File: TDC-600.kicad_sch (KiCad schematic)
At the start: 32 parts, among them J1 MSXCART1, J2 Conn_01x03_Male, J3 Conn_01x03_Male, J4 Conn_01x03_Male, J5 Conn_01x03_Male, J6 FDD Connector, J7 ROM_SWITCH, SW1 SW_Push, U1 AT28C256, U2 74LS04, U3 74LS138, U4 WDC37C65, Y1 16Mhz

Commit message: Routing Release 1.0
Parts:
- J1: footprint Roni Footprints:MSX_CART_SW_Official_3Holes -> Roni_Footprints:MSX_CART_SW_Official
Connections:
- net GNDREF: now also J1.41 (GND@1), J1.43 (GND@2)
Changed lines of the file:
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@@
   (junction (at 203.581 92.71) (diameter 0) (color 0 0 0 0)
   )
-  (junction (at 60.9838 78.867) (diameter 0) (color 0 0 0 0)
+  (junction (at 61.9643 78.867) (diameter 0) (color 0 0 0 0)
   )
   (junction (at 193.04 66.294) (diameter 0) (color 0 0 0 0)
@@
   (junction (at 193.04 71.374) (diameter 0) (color 0 0 0 0)
   )
+  (junction (at 66.04 78.74) (diameter 0) (color 0 0 0 0)
+  )
   (junction (at 228.346 125.857) (diameter 0) (color 0 0 0 0)
   )
@@
   )
   (junction (at 70.358 84.074) (diameter 0) (color 0 0 0 0)
-  )
-  (junction (at 60.96 78.74) (diameter 0) (color 0 0 0 0)
   )
   (junction (at 85.598 42.164) (diameter 0) (color 0 0 0 0)
@@
     (stroke (width 0) (type default) (color 0 0 0 0))
   )
-  (wire (pts (xy 58.928 78.867) (xy 60.9838 78.867))
-    (stroke (width 0) (type default) (color 0 0 0 0))
-  )
   (wire (pts (xy 129.286 105.664) (xy 121.666 105.664))
     (stroke (width 0) (type default) (color 0 0 0 0))
@@
     (stroke (width 0) (type default) (color 0 0 0 0))
   )
-  (wire (pts (xy 58.928 81.407) (xy 60.9838 81.407))
+  (wire (pts (xy 58.928 81.407) (xy 61.9643 81.407))
+    (stroke (width 0) (type default) (color 0 0 0 0))
+  )
+  (wire (pts (xy 66.04 78.867) (xy 66.04 78.74))
     (stroke (width 0) (type default) (color 0 0 0 0))
   )
@@
     (stroke (width 0) (type default) (color 0 0 0 0))
   )
-  (wire (pts (xy 60.9838 81.407) (xy 60.9838 78.867))
+  (wire (pts (xy 58.928 78.867) (xy 61.9643 78.867))
     (stroke (width 0) (type default) (color 0 0 0 0))
   )
@@
     (stroke (width 0) (type default) (color 0 0 0 0))
   )
+  (wire (pts (xy 61.9643 81.407) (xy 61.9643 78.867))
+    (stroke (width 0) (type default) (color 0 0 0 0))
+  )
   (wire (pts (xy 215.392 125.857) (xy 220.345 125.857))
     (stroke (width 0) (type default) (color 0 0 0 0))
@@
     (stroke (width 0) (type default) (color 0 0 0 0))
   )
+  (wire (pts (xy 61.9643 78.867) (xy 66.04 78.867))
+    (stroke (width 0) (type default) (color 0 0 0 0))
+  )
   (wire (pts (xy 165.354 145.161) (xy 178.054 145.161))
     (stroke (width 0) (type default) (color 0 0 0 0))
@@
     (stroke (width 0) (type default) (color 0 0 0 0))
   )
-  (wire (pts (xy 64.262 78.74) (xy 64.262 78.994))
-    (stroke (width 0) (type default) (color 0 0 0 0))
-  )
   (wire (pts (xy 122.174 132.588) (xy 122.174 130.048))
     (stroke (width 0) (type default) (color 0 0 0 0))
@@
   )
   (wire (pts (xy 108.204 137.668) (xy 109.474 137.668))
-    (stroke (width 0) (type default) (color 0 0 0 0))
-  )
-  (wire (pts (xy 60.96 78.74) (xy 64.262 78.74))
     (stroke (width 0) (type default) (color 0 0 0 0))
   )
@@
     (pin "1")
   )
-  (symbol (lib_id "power:GNDREF") (at 64.262 78.994 0) (unit 1)
-    (in_bom yes) (on_board yes) (fields_autoplaced)
-    (property "Reference" "#PWR01" (id 0) (at 64.262 85.344 0)
-      (effects (font (size 1 1)) hide)
-    )
-    (property "Value" "GNDREF" (id 1) (at 64.262 84.582 0)
-      (effects (font (size 1 1)) hide)
-    )
-    (property "Footprint" "" (id 2) (at 64.262 78.994 0)
-      (effects (font (size 1 1)) hide)
-    )
-    (property "Datasheet" "" (id 3) (at 64.262 78.994 0)
-      (effects (font (size 1 1)) hide)
-    )
-    (pin "1")
-  )
   (symbol (lib_id "power:GNDREF") (at 167.386 83.058 0) (unit 1)
     (in_bom yes) (on_board yes) (fields_autoplaced)
@@
       (effects (font (size 1 1)) hide)
     )
-    (property "Footprint" "Roni Footprints:MSX_CART_SW_Official_3Holes" (id 2) (at 43.688 58.547 0)
+    (property "Footprint" "Roni_Footprints:MSX_CART_SW_Official" (id 2) (at 43.688 58.547 0)
       (effects (font (size 1 1)) hide)
     )
@@
     (pin "7")
   )
+  (symbol (lib_id "power:GNDREF") (at 66.04 78.74 0) (unit 1)
+    (in_bom yes) (on_board yes) (fields_autoplaced)
+    (property "Reference" "#PWR?" (id 0) (at 66.04 85.09 0)
+      (effects (font (size 1 1)) hide)
+    )
+    (property "Value" "GNDREF" (id 1) (at 66.04 84.328 0)
+      (effects (font (size 1 1)) hide)
+    )
+    (property "Footprint" "" (id 2) (at 66.04 78.74 0)
+      (effects (font (size 1 1)) hide)
+    )
+    (property "Datasheet" "" (id 3) (at 66.04 78.74 0)
+      (effects (font (size 1 1)) hide)
+    )
+    (pin "1")
+  )
   (symbol (lib_id "74xx:74LS04") (at 251.206 50.8 0) (unit 1)
     (in_bom yes) (on_board yes)
@@
   )
   (symbol_instances
-    (path "/5fd49dc5-3ef7-42c3-ba98-39fb50cf0473"
-      (reference "#PWR01") (unit 1) (value "GNDREF") (footprint "")
-    )
     (path "/64de7322-3492-44c0-b600-8a8a1cbeb091"
       (reference "#PWR02") (unit 1) (value "+5V") (footprint "")
@@
       (reference "#PWR021") (unit 1) (value "+5V") (footprint "")
     )
+    (path "/f82b494c-be8d-4f2a-a5d0-8b689b314ae2"
+      (reference "#PWR?") (unit 1) (value "GNDREF") (footprint "")
+    )
     (path "/b16493d0-17e8-4588-8dc9-b6b9eb468398"
       (reference "C1") (unit 1) (value "10uF") (footprint "Capacitor_THT:CP_Radial_D4.0mm_P1.50mm")
@@
     )
     (path "/c88d69e7-0f10-442f-b4e9-d3ac6c8cb585"
-      (reference "J1") (unit 1) (value "MSXCART1") (footprint "Roni Footprints:MSX_CART_SW_Official_3Holes")
+      (reference "J1") (unit 1) (value "MSXCART1") (footprint "Roni_Footprints:MSX_CART_SW_Official")
     )
     (path "/3712ef9a-3384-4ffe-bc7d-57032448a0fc"

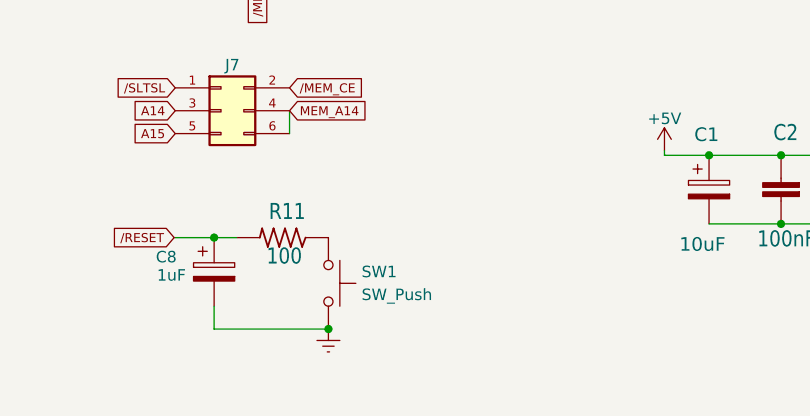
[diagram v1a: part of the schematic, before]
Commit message: Routing complete for Rev 1.0
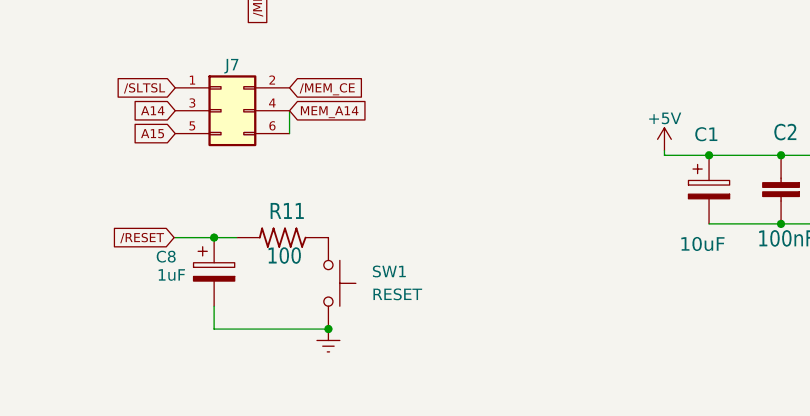
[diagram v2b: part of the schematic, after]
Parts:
- J6: footprint Connector_PinHeader_2.54mm:PinHeader_2x17_P2.54mm_Horizontal -> Connector_PinHeader_2.54mm:PinHeader_2x17_P2.54mm_Vertical
- J7: footprint Connector_PinHeader_2.54mm:PinHeader_2x03_P2.54mm_Horizontal -> Connector_PinHeader_2.54mm:PinHeader_2x03_P2.54mm_Vertical
- SW1: value SW_Push -> RESET
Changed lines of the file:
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@@
     (property "Reference" "J6" (id 0) (at 199.644 25.273 0))
     (property "Value" "FDD Connector" (id 1) (at 200.025 27.686 0))
-    (property "Footprint" "Connector_PinHeader_2.54mm:PinHeader_2x17_P2.54mm_Horizontal" (id 2) (at 198.12 51.054 0)
+    (property "Footprint" "Connector_PinHeader_2.54mm:PinHeader_2x17_P2.54mm_Vertical" (id 2) (at 198.12 51.054 0)
       (effects (font (size 1.27 1.27)) hide)
     )
@@
       (effects (font (size 1 1)) hide)
     )
-    (property "Footprint" "Connector_PinHeader_2.54mm:PinHeader_2x03_P2.54mm_Horizontal" (id 2) (at 166.116 120.904 0)
+    (property "Footprint" "Connector_PinHeader_2.54mm:PinHeader_2x03_P2.54mm_Vertical" (id 2) (at 166.116 120.904 0)
       (effects (font (size 1 1)) hide)
     )
@@
   (symbol (lib_id "Switch:SW_Push") (at 178.054 140.081 270) (unit 1)
     (in_bom yes) (on_board yes) (fields_autoplaced)
-    (property "Reference" "SW1" (id 0) (at 181.737 138.8109 90)
+    (property "Reference" "SW1" (id 0) (at 182.88 138.8109 90)
       (effects (font (size 1.27 1.27)) (justify left))
     )
-    (property "Value" "SW_Push" (id 1) (at 181.737 141.3509 90)
+    (property "Value" "RESET" (id 1) (at 182.88 141.3509 90)
       (effects (font (size 1.27 1.27)) (justify left))
     )
@@
   (symbol (lib_id "power:GNDREF") (at 66.04 78.74 0) (unit 1)
     (in_bom yes) (on_board yes) (fields_autoplaced)
-    (property "Reference" "#PWR?" (id 0) (at 66.04 85.09 0)
+    (property "Reference" "#PWR0101" (id 0) (at 66.04 85.09 0)
       (effects (font (size 1 1)) hide)
     )
@@
     )
     (path "/f82b494c-be8d-4f2a-a5d0-8b689b314ae2"
-      (reference "#PWR?") (unit 1) (value "GNDREF") (footprint "")
+      (reference "#PWR0101") (unit 1) (value "GNDREF") (footprint "")
     )
     (path "/b16493d0-17e8-4588-8dc9-b6b9eb468398"
@@
     )
     (path "/170ecc87-1c9d-41f1-84c0-57d7f7bcd9a5"
-      (reference "J6") (unit 1) (value "FDD Connector") (footprint "Connector_PinHeader_2.54mm:PinHeader_2x17_P2.54mm_Horizontal")
+      (reference "J6") (unit 1) (value "FDD Connector") (footprint "Connector_PinHeader_2.54mm:PinHeader_2x17_P2.54mm_Vertical")
     )
     (path "/1c52b236-3822-49fa-aef3-26d81bf9a744"
-      (reference "J7") (unit 1) (value "ROM_SWITCH") (footprint "Connector_PinHeader_2.54mm:PinHeader_2x03_P2.54mm_Horizontal")
+      (reference "J7") (unit 1) (value "ROM_SWITCH") (footprint "Connector_PinHeader_2.54mm:PinHeader_2x03_P2.54mm_Vertical")
     )
     (path "/842d9f0d-7fa3-40b0-801b-9a2ab6d14708"
@@
     )
     (path "/ce6f7dd5-f181-425a-96c4-049847557d3a"
-      (reference "SW1") (unit 1) (value "SW_Push") (footprint "Button_Switch_THT:SW_Tactile_SPST_Angled_PTS645Vx31-2LFS")
+      (reference "SW1") (unit 1) (value "RESET") (footprint "Button_Switch_THT:SW_Tactile_SPST_Angled_PTS645Vx31-2LFS")
     )
     (path "/0026b233-4b7a-445d-884f-ac187d60d3c9"
